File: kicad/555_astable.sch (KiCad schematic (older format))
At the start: 10 parts, among them U1 555

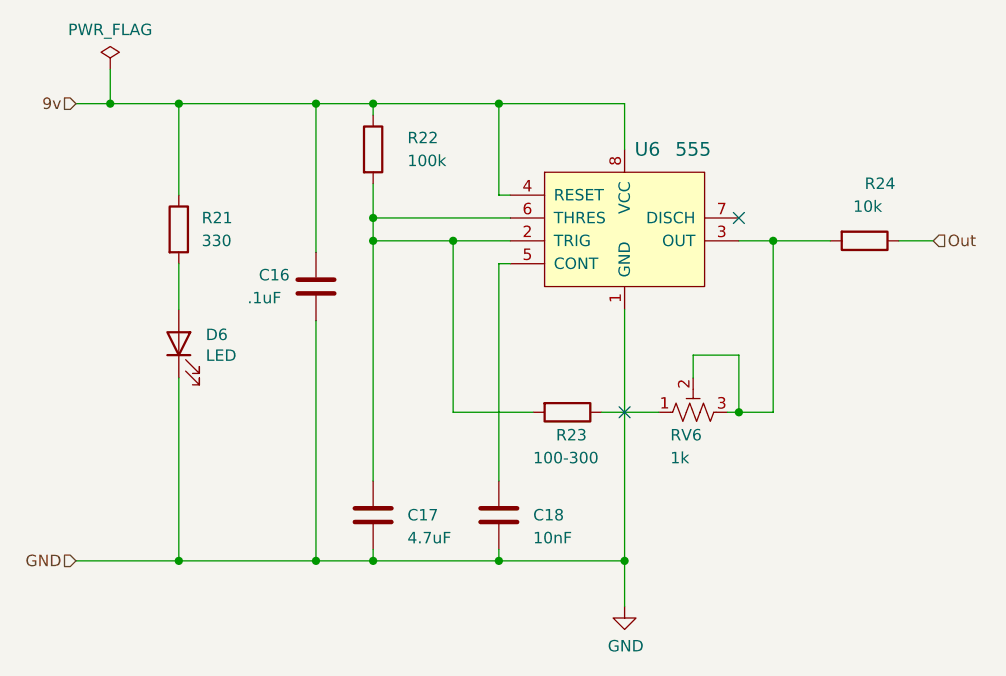
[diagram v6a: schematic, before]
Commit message: Update PCB and schematic
* Finalize timing R to 100
* Drop LED ohms to 220
* Add missing 1k value to RV21
* Fix timing cap and 7805 label placements
* Widen speaker and battery relief holes
* Re-label SPK and BAT
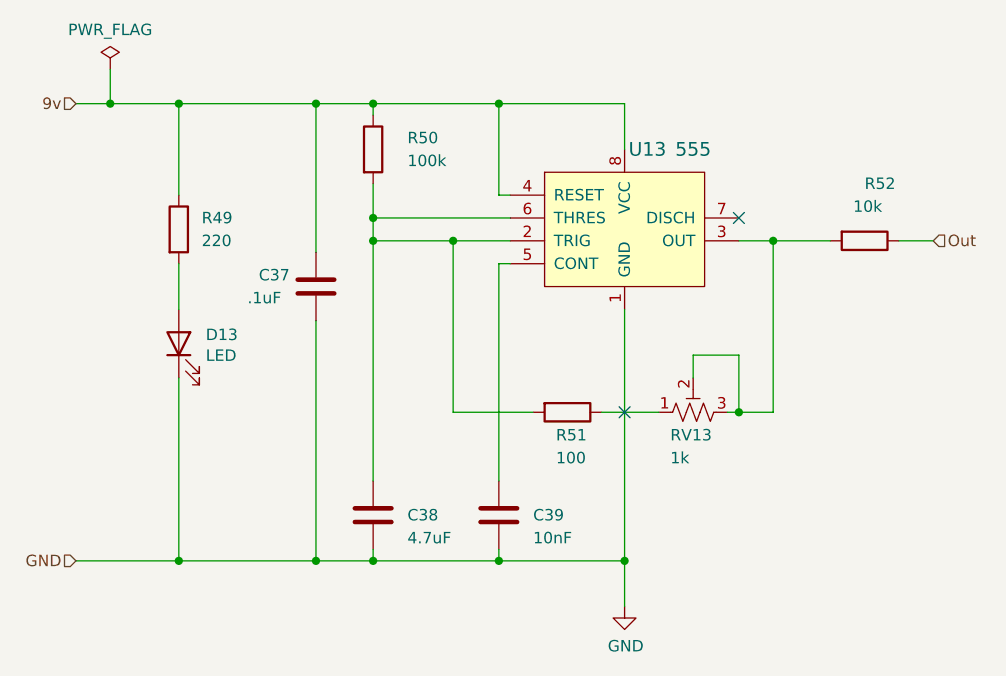
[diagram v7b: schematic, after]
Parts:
- R1: value 330 -> 220
- R3: value 100-300 -> 100
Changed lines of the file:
@@
 $Descr A4 11693 8268
 encoding utf-8
-Sheet 7 22
+Sheet 14 22
 Title ""
 Date ""
@@
 AR Path="/5F842C45/60F6A68E" Ref="R74"  Part="1"
 AR Path="/5F842C61/60F6A68E" Ref="R78"  Part="1"
-F 0 "R22" H 4750 3500 50  0000 L CNN
+F 0 "R50" H 4750 3500 50  0000 L CNN
 F 1 "100k" H 4750 3400 50  0000 L CNN
 F 2 "Resistor_THT:R_Axial_DIN0207_L6.3mm_D2.5mm_P2.54mm_Vertical" V 4530 3450 50  0001 C CNN
@@
 AR Path="/5F842C45/60F6EAC0" Ref="C55"  Part="1"
 AR Path="/5F842C61/60F6EAC0" Ref="C58"  Part="1"
-F 0 "C16" H 4100 4100 50  0000 L CNN
+F 0 "C37" H 4100 4100 50  0000 L CNN
 F 1 ".1uF" H 4050 4000 50  0000 L CNN
 F 2 "Capacitor_THT:C_Disc_D5.0mm_W2.5mm_P5.00mm" H 4388 3900 50  0001 C CNN
@@
 AR Path="/5F842C45/60F6A6DA" Ref="U19"  Part="1"
 AR Path="/5F842C61/60F6A6DA" Ref="U20"  Part="1"
-F 0 "U6" H 5800 4050 60  0000 C CNN
+F 0 "U13" H 5800 4050 60  0000 C CNN
 F 1 "555" H 6000 4050 60  0000 C CNN
 F 2 "Package_DIP:DIP-8_W7.62mm" H 5900 3950 60  0001 L CNN
@@
 AR Path="/5F842C45/60F6A6C5" Ref="RV19"  Part="1"
 AR Path="/5F842C61/60F6A6C5" Ref="RV20"  Part="1"
-F 0 "RV6" V 5900 4700 50  0000 R CNN
+F 0 "RV13" V 5900 4700 50  0000 R CNN
 F 1 "1k" V 5800 4700 50  0000 R CNN
 F 2 "Potentiometer_THT:Potentiometer_Piher_PT-6-V_Vertical" H 6000 4600 50  0001 C CNN
@@
 AR Path="/5F842C45/5EFAE830" Ref="R76"  Part="1"
 AR Path="/5F842C61/5EFAE830" Ref="R80"  Part="1"
-F 0 "R24" V 6500 3850 50  0000 L CNN
+F 0 "R52" V 6500 3850 50  0000 L CNN
 F 1 "10k" V 6600 3800 50  0000 L CNN
 F 2 "Resistor_THT:R_Axial_DIN0207_L6.3mm_D2.5mm_P2.54mm_Vertical" V 6680 3850 50  0001 C CNN
@@
 AR Path="/5F842C45/5F127BEF" Ref="D19"  Part="1"
 AR Path="/5F842C61/5F127BEF" Ref="D20"  Part="1"
-F 0 "D6" V 3789 4182 50  0000 R CNN
+F 0 "D13" V 3789 4182 50  0000 R CNN
 F 1 "LED" V 3698 4182 50  0000 R CNN
 F 2 "LED_THT:LED_D5.0mm" H 3750 4300 50  0001 C CNN
@@
 AR Path="/5F842C45/5F127BF5" Ref="R73"  Part="1"
 AR Path="/5F842C61/5F127BF5" Ref="R77"  Part="1"
-F 0 "R21" H 3850 3850 50  0000 L CNN
-F 1 "330" H 3850 3750 50  0000 L CNN
+F 0 "R49" H 3850 3850 50  0000 L CNN
+F 1 "220" H 3850 3750 50  0000 L CNN
 F 2 "Resistor_THT:R_Axial_DIN0207_L6.3mm_D2.5mm_P2.54mm_Vertical" V 3680 3800 50  0001 C CNN
 F 3 "~" H 3750 3800 50  0001 C CNN
@@
 AR Path="/5F842C45/60F6A6A0" Ref="C57"  Part="1"
 AR Path="/5F842C61/60F6A6A0" Ref="C60"  Part="1"
-F 0 "C18" H 5300 5050 50  0000 L CNN
+F 0 "C39" H 5300 5050 50  0000 L CNN
 F 1 "10nF" H 5300 4950 50  0000 L CNN
 F 2 "Capacitor_THT:C_Disc_D5.0mm_W2.5mm_P5.00mm" H 5188 4900 50  0001 C CNN
@@
 AR Path="/5F842C45/60F6A69A" Ref="C56"  Part="1"
 AR Path="/5F842C61/60F6A69A" Ref="C59"  Part="1"
-F 0 "C17" H 4750 5050 50  0000 L CNN
+F 0 "C38" H 4750 5050 50  0000 L CNN
 F 1 "4.7uF" H 4750 4950 50  0000 L CNN
 F 2 "Capacitor_THT:CP_Radial_D5.0mm_P2.00mm" H 4638 4900 50  0001 C CNN
@@
 AR Path="/5F842C45/5F3F39A8" Ref="R75"  Part="1"
 AR Path="/5F842C61/5F3F39A8" Ref="R79"  Part="1"
-F 0 "R23" V 5550 4550 50  0000 L CNN
-F 1 "100-300" V 5650 4450 50  0000 L CNN
+F 0 "R51" V 5550 4550 50  0000 L CNN
+F 1 "100" V 5650 4550 50  0000 L CNN
 F 2 "Resistor_THT:R_Axial_DIN0207_L6.3mm_D2.5mm_P2.54mm_Vertical" V 5380 4600 50  0001 C CNN
 F 3 "~" H 5450 4600 50  0001 C CNN

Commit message: Tidy schematic
* Remove vestigial comments
* Fix odd 555 sheet name
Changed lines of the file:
@@
 $Descr A4 11693 8268
 encoding utf-8
-Sheet 14 22
+Sheet 2 22
 Title ""
 Date ""
@@
 AR Path="/5F842C45/60F6A68E" Ref="R74"  Part="1"
 AR Path="/5F842C61/60F6A68E" Ref="R78"  Part="1"
-F 0 "R50" H 4750 3500 50  0000 L CNN
+F 0 "R2" H 4750 3500 50  0000 L CNN
 F 1 "100k" H 4750 3400 50  0000 L CNN
 F 2 "Resistor_THT:R_Axial_DIN0207_L6.3mm_D2.5mm_P2.54mm_Vertical" V 4530 3450 50  0001 C CNN
@@
 AR Path="/5F842C45/60F6EAC0" Ref="C55"  Part="1"
 AR Path="/5F842C61/60F6EAC0" Ref="C58"  Part="1"
-F 0 "C37" H 4100 4100 50  0000 L CNN
+F 0 "C1" H 4100 4100 50  0000 L CNN
 F 1 ".1uF" H 4050 4000 50  0000 L CNN
 F 2 "Capacitor_THT:C_Disc_D5.0mm_W2.5mm_P5.00mm" H 4388 3900 50  0001 C CNN
@@
 AR Path="/5F842C45/60F6A6DA" Ref="U19"  Part="1"
 AR Path="/5F842C61/60F6A6DA" Ref="U20"  Part="1"
-F 0 "U13" H 5800 4050 60  0000 C CNN
+F 0 "U1" H 5800 4050 60  0000 C CNN
 F 1 "555" H 6000 4050 60  0000 C CNN
 F 2 "Package_DIP:DIP-8_W7.62mm" H 5900 3950 60  0001 L CNN
@@
 AR Path="/5F842C45/60F6A6C5" Ref="RV19"  Part="1"
 AR Path="/5F842C61/60F6A6C5" Ref="RV20"  Part="1"
-F 0 "RV13" V 5900 4700 50  0000 R CNN
+F 0 "RV1" V 5900 4700 50  0000 R CNN
 F 1 "1k" V 5800 4700 50  0000 R CNN
 F 2 "Potentiometer_THT:Potentiometer_Piher_PT-6-V_Vertical" H 6000 4600 50  0001 C CNN
@@
 AR Path="/5F842C45/5EFAE830" Ref="R76"  Part="1"
 AR Path="/5F842C61/5EFAE830" Ref="R80"  Part="1"
-F 0 "R52" V 6500 3850 50  0000 L CNN
+F 0 "R4" V 6500 3850 50  0000 L CNN
 F 1 "10k" V 6600 3800 50  0000 L CNN
 F 2 "Resistor_THT:R_Axial_DIN0207_L6.3mm_D2.5mm_P2.54mm_Vertical" V 6680 3850 50  0001 C CNN
@@
 AR Path="/5F842C45/5F127BEF" Ref="D19"  Part="1"
 AR Path="/5F842C61/5F127BEF" Ref="D20"  Part="1"
-F 0 "D13" V 3789 4182 50  0000 R CNN
+F 0 "D1" V 3789 4182 50  0000 R CNN
 F 1 "LED" V 3698 4182 50  0000 R CNN
 F 2 "LED_THT:LED_D5.0mm" H 3750 4300 50  0001 C CNN
@@
 AR Path="/5F842C45/5F127BF5" Ref="R73"  Part="1"
 AR Path="/5F842C61/5F127BF5" Ref="R77"  Part="1"
-F 0 "R49" H 3850 3850 50  0000 L CNN
+F 0 "R1" H 3850 3850 50  0000 L CNN
 F 1 "220" H 3850 3750 50  0000 L CNN
 F 2 "Resistor_THT:R_Axial_DIN0207_L6.3mm_D2.5mm_P2.54mm_Vertical" V 3680 3800 50  0001 C CNN
@@
 AR Path="/5F842C45/60F6A6A0" Ref="C57"  Part="1"
 AR Path="/5F842C61/60F6A6A0" Ref="C60"  Part="1"
-F 0 "C39" H 5300 5050 50  0000 L CNN
+F 0 "C3" H 5300 5050 50  0000 L CNN
 F 1 "10nF" H 5300 4950 50  0000 L CNN
 F 2 "Capacitor_THT:C_Disc_D5.0mm_W2.5mm_P5.00mm" H 5188 4900 50  0001 C CNN
@@
 AR Path="/5F842C45/60F6A69A" Ref="C56"  Part="1"
 AR Path="/5F842C61/60F6A69A" Ref="C59"  Part="1"
-F 0 "C38" H 4750 5050 50  0000 L CNN
+F 0 "C2" H 4750 5050 50  0000 L CNN
 F 1 "4.7uF" H 4750 4950 50  0000 L CNN
 F 2 "Capacitor_THT:CP_Radial_D5.0mm_P2.00mm" H 4638 4900 50  0001 C CNN
@@
 AR Path="/5F842C45/5F3F39A8" Ref="R75"  Part="1"
 AR Path="/5F842C61/5F3F39A8" Ref="R79"  Part="1"
-F 0 "R51" V 5550 4550 50  0000 L CNN
+F 0 "R3" V 5550 4550 50  0000 L CNN
 F 1 "100" V 5650 4550 50  0000 L CNN
 F 2 "Resistor_THT:R_Axial_DIN0207_L6.3mm_D2.5mm_P2.54mm_Vertical" V 5380 4600 50  0001 C CNN
